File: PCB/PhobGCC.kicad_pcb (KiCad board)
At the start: 2 copper layers, 125.5 x 72.9 mm, 47 parts, among them J1 Conn_01x06_Female, J2 Conn_01x04_Female, J3 Conn_01x01_Male, J4 Conn_01x01_Male, J6 10118194-0001LF, SW1 A, SW10 Dup, SW11 Dright, SW12 Ddown, SW2 B, SW3 X, SW4 Y, SW5 Start, SW6 L, SW7 R, SW8 1825027-5, SW9 Dleft, U1 Teensy3.2, U2 2x DRV5053CAQLPGM Hall Effect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, U3 XC6220B331MR

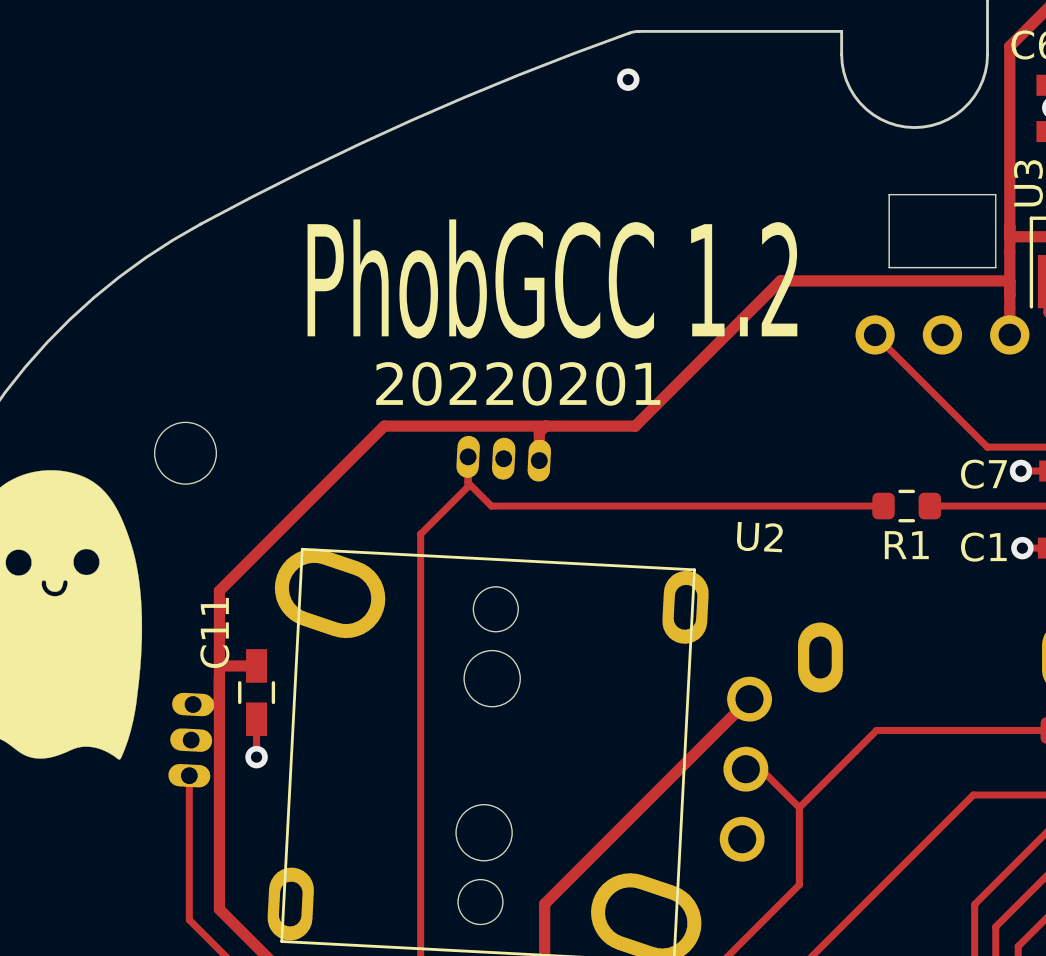
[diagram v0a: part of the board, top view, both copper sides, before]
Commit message: Reverted the kicad and gerber files back to the 1.1 board version so they match up with the manufacturing files for JLC
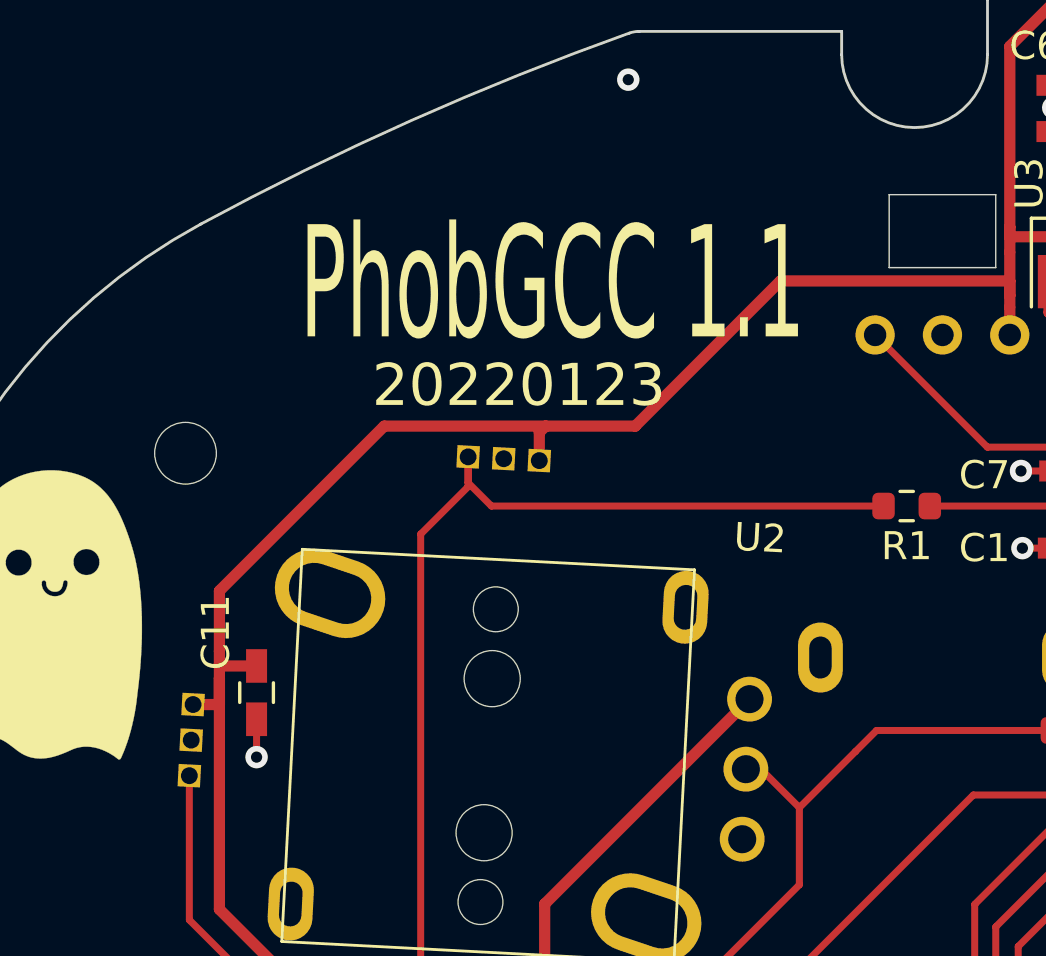
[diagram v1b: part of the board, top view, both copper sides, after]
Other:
- board text added: "20220123"
- board text added: "PhobGCC 1.1"
- board text removed: "20220201"
- board text removed: "PhobGCC 1.2"
